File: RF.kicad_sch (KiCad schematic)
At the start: 14 parts, among them J10 SMA_Edge, J9 SMA_Edge, U11 MAX-M10S, U12 E22-900MM22S

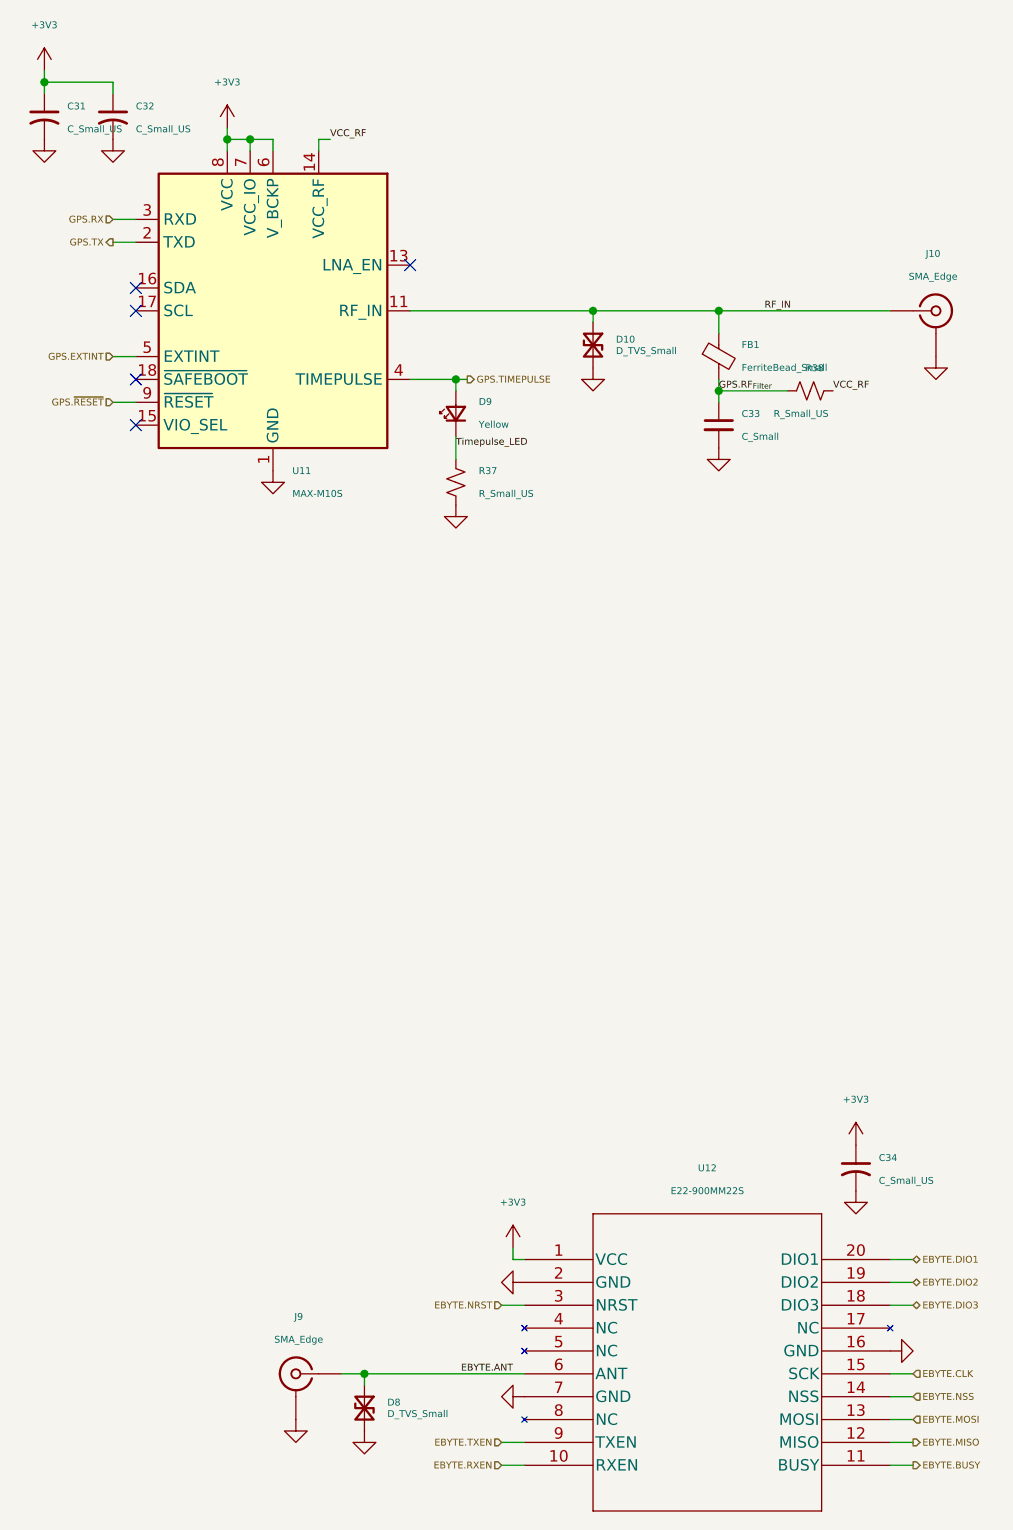
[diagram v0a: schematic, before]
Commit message: Changed some of the silkscreen, and added some LEDs attached to some gpio
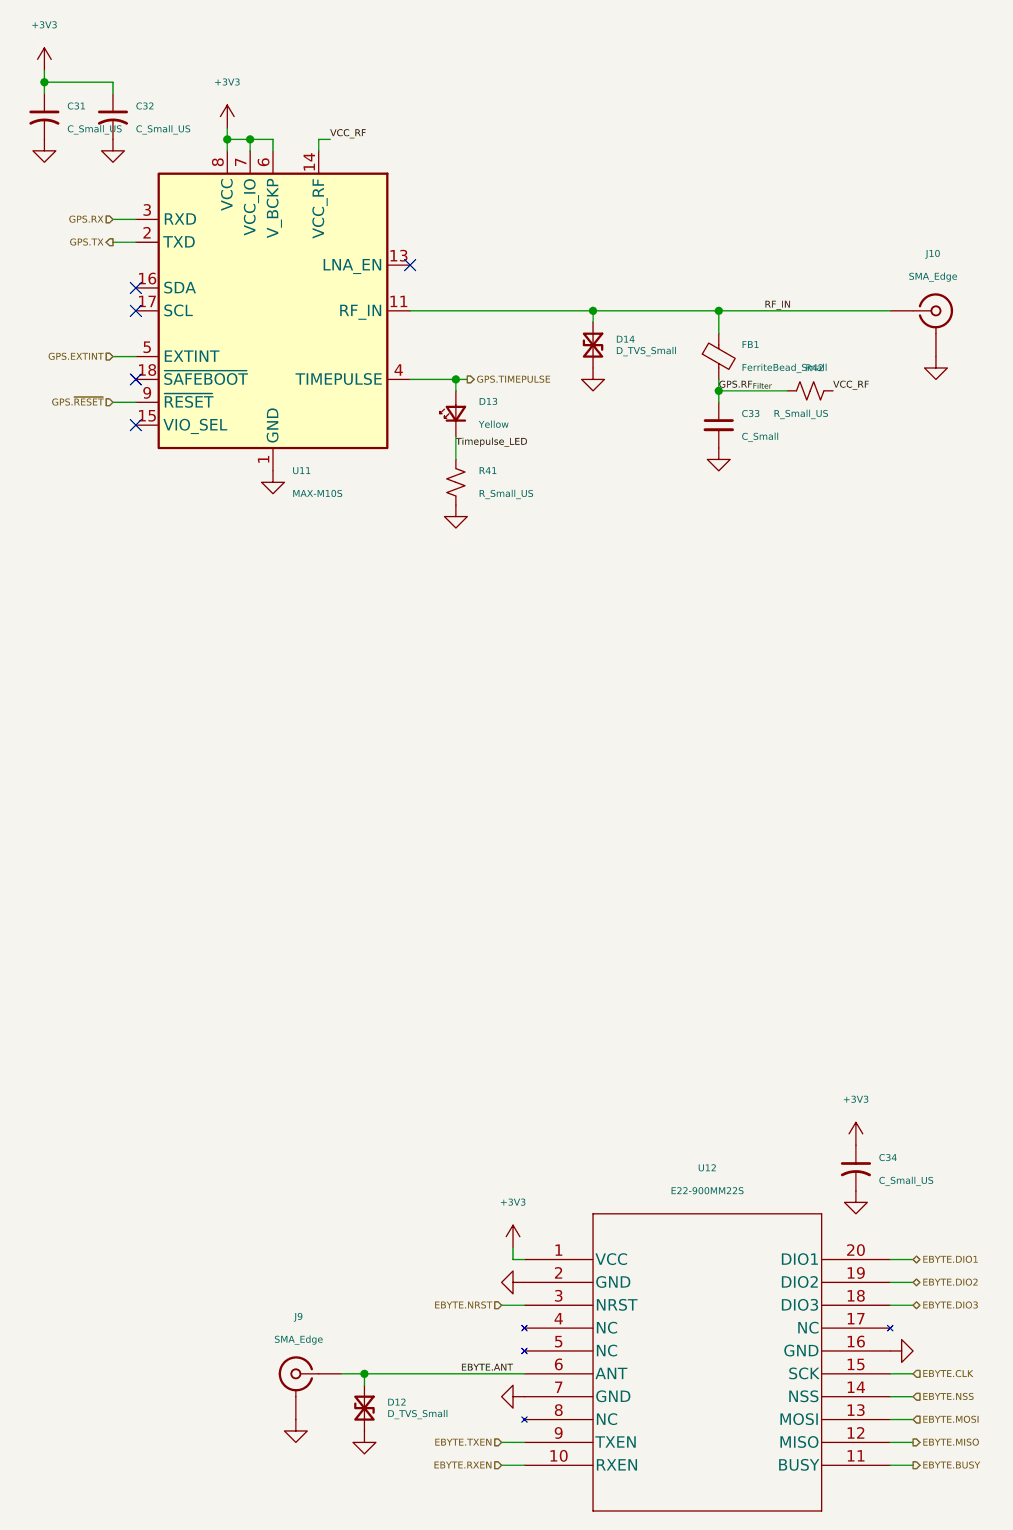
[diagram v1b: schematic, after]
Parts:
- renumbered D8 to D12, D9 to D13, D10 to D14, R37 to R41, R38 to R42
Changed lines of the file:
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@@
 		(dnp no)
 		(fields_autoplaced yes)
-		(property "Reference" "#PWR0126"
+		(property "Reference" "#PWR0131"
 			(at 83.82 175.26 0)
 			(hide yes)
@@
 			(project "LSR_FLCM0001_A03"
 				(path "/1e96c69b-f36f-4762-8445-55c423e1825d/3ad2e3ca-d35b-487a-a973-24fd15701930/afa4768e-6edd-4ec3-ad27-4eb29bbcd0f3"
-					(reference "#PWR0126")
+					(reference "#PWR0131")
 					(unit 1)
 				)
@@
 		(in_pos_files yes)
 		(dnp no)
-		(property "Reference" "R37"
+		(property "Reference" "R41"
 			(at 85.09 72.3899 0)
 			(show_name no)
@@
 			(project "LSR_FLCM0001_A03"
 				(path "/1e96c69b-f36f-4762-8445-55c423e1825d/3ad2e3ca-d35b-487a-a973-24fd15701930/afa4768e-6edd-4ec3-ad27-4eb29bbcd0f3"
-					(reference "R37")
+					(reference "R41")
 					(unit 1)
 					(variant
@@
 		(dnp no)
 		(fields_autoplaced yes)
-		(property "Reference" "D9"
+		(property "Reference" "D13"
 			(at 85.09 64.7064 90)
 			(show_name no)
@@
 			(project "LSR_FLCM0001_A03"
 				(path "/1e96c69b-f36f-4762-8445-55c423e1825d/3ad2e3ca-d35b-487a-a973-24fd15701930/afa4768e-6edd-4ec3-ad27-4eb29bbcd0f3"
-					(reference "D9")
+					(reference "D13")
 					(unit 1)
 					(variant
@@
 		(dnp no)
 		(fields_autoplaced yes)
-		(property "Reference" "#PWR0129"
+		(property "Reference" "#PWR0134"
 			(at 127 151.13 0)
 			(hide yes)
@@
 			(project "LSR_FLCM0001_A03"
 				(path "/1e96c69b-f36f-4762-8445-55c423e1825d/3ad2e3ca-d35b-487a-a973-24fd15701930/afa4768e-6edd-4ec3-ad27-4eb29bbcd0f3"
-					(reference "#PWR0129")
+					(reference "#PWR0134")
 					(unit 1)
 				)
@@
 		(dnp no)
 		(fields_autoplaced yes)
-		(property "Reference" "#PWR0121"
+		(property "Reference" "#PWR0126"
 			(at 64.77 184.15 0)
 			(hide yes)
@@
 			(project "LSR_FLCM0001_A03"
 				(path "/1e96c69b-f36f-4762-8445-55c423e1825d/3ad2e3ca-d35b-487a-a973-24fd15701930/afa4768e-6edd-4ec3-ad27-4eb29bbcd0f3"
-					(reference "#PWR0121")
+					(reference "#PWR0126")
 					(unit 1)
 				)
@@
 		(dnp no)
 		(fields_autoplaced yes)
-		(property "Reference" "D8"
+		(property "Reference" "D12"
 			(at 74.93 175.895 90)
 			(show_name no)
@@
 			(project "LSR_FLCM0001_A03"
 				(path "/1e96c69b-f36f-4762-8445-55c423e1825d/3ad2e3ca-d35b-487a-a973-24fd15701930/afa4768e-6edd-4ec3-ad27-4eb29bbcd0f3"
-					(reference "D8")
+					(reference "D12")
 					(unit 1)
 					(variant
@@
 		(dnp no)
 		(fields_autoplaced yes)
-		(property "Reference" "#PWR0128"
+		(property "Reference" "#PWR0133"
 			(at 111.76 76.2 0)
 			(hide yes)
@@
 			(project "LSR_FLCM0001_A03"
 				(path "/1e96c69b-f36f-4762-8445-55c423e1825d/3ad2e3ca-d35b-487a-a973-24fd15701930/afa4768e-6edd-4ec3-ad27-4eb29bbcd0f3"
-					(reference "#PWR0128")
+					(reference "#PWR0133")
 					(unit 1)
 				)
@@
 		(dnp no)
 		(fields_autoplaced yes)
-		(property "Reference" "#PWR0127"
+		(property "Reference" "#PWR0132"
 			(at 97.79 67.31 0)
 			(hide yes)
@@
 			(project "LSR_FLCM0001_A03"
 				(path "/1e96c69b-f36f-4762-8445-55c423e1825d/3ad2e3ca-d35b-487a-a973-24fd15701930/afa4768e-6edd-4ec3-ad27-4eb29bbcd0f3"
-					(reference "#PWR0127")
+					(reference "#PWR0132")
 					(unit 1)
 				)
@@
 		(dnp no)
 		(fields_autoplaced yes)
-		(property "Reference" "#PWR0117"
+		(property "Reference" "#PWR0122"
 			(at 36.83 41.91 0)
 			(hide yes)
@@
 			(project "LSR_FLCM0001_A03"
 				(path "/1e96c69b-f36f-4762-8445-55c423e1825d/3ad2e3ca-d35b-487a-a973-24fd15701930/afa4768e-6edd-4ec3-ad27-4eb29bbcd0f3"
-					(reference "#PWR0117")
+					(reference "#PWR0122")
 					(unit 1)
 				)
@@
 		(dnp no)
 		(fields_autoplaced yes)
-		(property "Reference" "#PWR0119"
+		(property "Reference" "#PWR0124"
 			(at 57.15 38.1 0)
 			(hide yes)
@@
 			(project "LSR_FLCM0001_A03"
 				(path "/1e96c69b-f36f-4762-8445-55c423e1825d/3ad2e3ca-d35b-487a-a973-24fd15701930/afa4768e-6edd-4ec3-ad27-4eb29bbcd0f3"
-					(reference "#PWR0119")
+					(reference "#PWR0124")
 					(unit 1)
 				)
@@
 		(dnp no)
 		(fields_autoplaced yes)
-		(property "Reference" "#PWR0120"
+		(property "Reference" "#PWR0125"
 			(at 62.23 78.74 0)
 			(hide yes)
@@
 			(project "LSR_FLCM0001_A03"
 				(path "/1e96c69b-f36f-4762-8445-55c423e1825d/3ad2e3ca-d35b-487a-a973-24fd15701930/afa4768e-6edd-4ec3-ad27-4eb29bbcd0f3"
-					(reference "#PWR0120")
+					(reference "#PWR0125")
 					(unit 1)
 				)
@@
 		(dnp no)
 		(fields_autoplaced yes)
-		(property "Reference" "#PWR0118"
+		(property "Reference" "#PWR0123"
 			(at 44.45 41.91 0)
 			(hide yes)
@@
 			(project "LSR_FLCM0001_A03"
 				(path "/1e96c69b-f36f-4762-8445-55c423e1825d/3ad2e3ca-d35b-487a-a973-24fd15701930/afa4768e-6edd-4ec3-ad27-4eb29bbcd0f3"
-					(reference "#PWR0118")
+					(reference "#PWR0123")
 					(unit 1)
 				)
@@
 		(dnp no)
 		(fields_autoplaced yes)
-		(property "Reference" "#PWR0130"
+		(property "Reference" "#PWR0135"
 			(at 127 158.75 0)
 			(hide yes)
@@
 			(project "LSR_FLCM0001_A03"
 				(path "/1e96c69b-f36f-4762-8445-55c423e1825d/3ad2e3ca-d35b-487a-a973-24fd15701930/afa4768e-6edd-4ec3-ad27-4eb29bbcd0f3"
-					(reference "#PWR0130")
+					(reference "#PWR0135")
 					(unit 1)
 				)
@@
 		(dnp no)
 		(fields_autoplaced yes)
-		(property "Reference" "#PWR0125"
+		(property "Reference" "#PWR0130"
 			(at 83.82 162.56 0)
 			(hide yes)
@@
 			(project "LSR_FLCM0001_A03"
 				(path "/1e96c69b-f36f-4762-8445-55c423e1825d/3ad2e3ca-d35b-487a-a973-24fd15701930/afa4768e-6edd-4ec3-ad27-4eb29bbcd0f3"
-					(reference "#PWR0125")
+					(reference "#PWR0130")
 					(unit 1)
 				)
@@
 		(dnp no)
 		(fields_autoplaced yes)
-		(property "Reference" "#PWR0123"
+		(property "Reference" "#PWR0128"
 			(at 82.55 82.55 0)
 			(hide yes)
@@
 			(project "LSR_FLCM0001_A03"
 				(path "/1e96c69b-f36f-4762-8445-55c423e1825d/3ad2e3ca-d35b-487a-a973-24fd15701930/afa4768e-6edd-4ec3-ad27-4eb29bbcd0f3"
-					(reference "#PWR0123")
+					(reference "#PWR0128")
 					(unit 1)
 				)
@@
 		(dnp no)
 		(fields_autoplaced yes)
-		(property "Reference" "D10"
+		(property "Reference" "D14"
 			(at 100.33 57.785 90)
 			(show_name no)
@@
 			(project "LSR_FLCM0001_A03"
 				(path "/1e96c69b-f36f-4762-8445-55c423e1825d/3ad2e3ca-d35b-487a-a973-24fd15701930/afa4768e-6edd-4ec3-ad27-4eb29bbcd0f3"
-					(reference "D10")
+					(reference "D14")
 					(unit 1)
 					(variant
@@
 		(in_pos_files yes)
 		(dnp no)
-		(property "Reference" "R38"
+		(property "Reference" "R42"
 			(at 123.444 60.96 90)
 			(show_name no)
@@
 			(project "LSR_FLCM0001_A03"
 				(path "/1e96c69b-f36f-4762-8445-55c423e1825d/3ad2e3ca-d35b-487a-a973-24fd15701930/afa4768e-6edd-4ec3-ad27-4eb29bbcd0f3"
-					(reference "R38")
+					(reference "R42")
 					(unit 1)
 					(variant
@@
 		(dnp no)
 		(fields_autoplaced yes)
-		(property "Reference" "#PWR0116"
+		(property "Reference" "#PWR0121"
 			(at 36.83 31.75 0)
 			(hide yes)
@@
 			(project "LSR_FLCM0001_A03"
 				(path "/1e96c69b-f36f-4762-8445-55c423e1825d/3ad2e3ca-d35b-487a-a973-24fd15701930/afa4768e-6edd-4ec3-ad27-4eb29bbcd0f3"
-					(reference "#PWR0116")
+					(reference "#PWR0121")
 					(unit 1)
 				)
@@
 		(dnp no)
 		(fields_autoplaced yes)
-		(property "Reference" "#PWR0124"
+		(property "Reference" "#PWR0129"
 			(at 88.9 162.56 0)
 			(hide yes)
@@
 			(project "LSR_FLCM0001_A03"
 				(path "/1e96c69b-f36f-4762-8445-55c423e1825d/3ad2e3ca-d35b-487a-a973-24fd15701930/afa4768e-6edd-4ec3-ad27-4eb29bbcd0f3"
-					(reference "#PWR0124")
+					(reference "#PWR0129")
 					(unit 1)
 				)
@@
 		(dnp no)
 		(fields_autoplaced yes)
-		(property "Reference" "#PWR0132"
+		(property "Reference" "#PWR0137"
 			(at 135.89 66.04 0)
 			(hide yes)
@@
 			(project "LSR_FLCM0001_A03"
 				(path "/1e96c69b-f36f-4762-8445-55c423e1825d/3ad2e3ca-d35b-487a-a973-24fd15701930/afa4768e-6edd-4ec3-ad27-4eb29bbcd0f3"
-					(reference "#PWR0132")
+					(reference "#PWR0137")
 					(unit 1)
 				)
@@
 		(dnp no)
 		(fields_autoplaced yes)
-		(property "Reference" "#PWR0122"
+		(property "Reference" "#PWR0127"
 			(at 72.39 185.42 0)
 			(hide yes)
@@
 			(project "LSR_FLCM0001_A03"
 				(path "/1e96c69b-f36f-4762-8445-55c423e1825d/3ad2e3ca-d35b-487a-a973-24fd15701930/afa4768e-6edd-4ec3-ad27-4eb29bbcd0f3"
-					(reference "#PWR0122")
+					(reference "#PWR0127")
 					(unit 1)
 				)
@@
 		(dnp no)
 		(fields_autoplaced yes)
-		(property "Reference" "#PWR0131"
+		(property "Reference" "#PWR0136"
 			(at 137.16 170.18 0)
 			(hide yes)
@@
 			(project "LSR_FLCM0001_A03"
 				(path "/1e96c69b-f36f-4762-8445-55c423e1825d/3ad2e3ca-d35b-487a-a973-24fd15701930/afa4768e-6edd-4ec3-ad27-4eb29bbcd0f3"
-					(reference "#PWR0131")
+					(reference "#PWR0136")
 					(unit 1)
 				)
